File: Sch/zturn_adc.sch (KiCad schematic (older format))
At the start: 0 parts

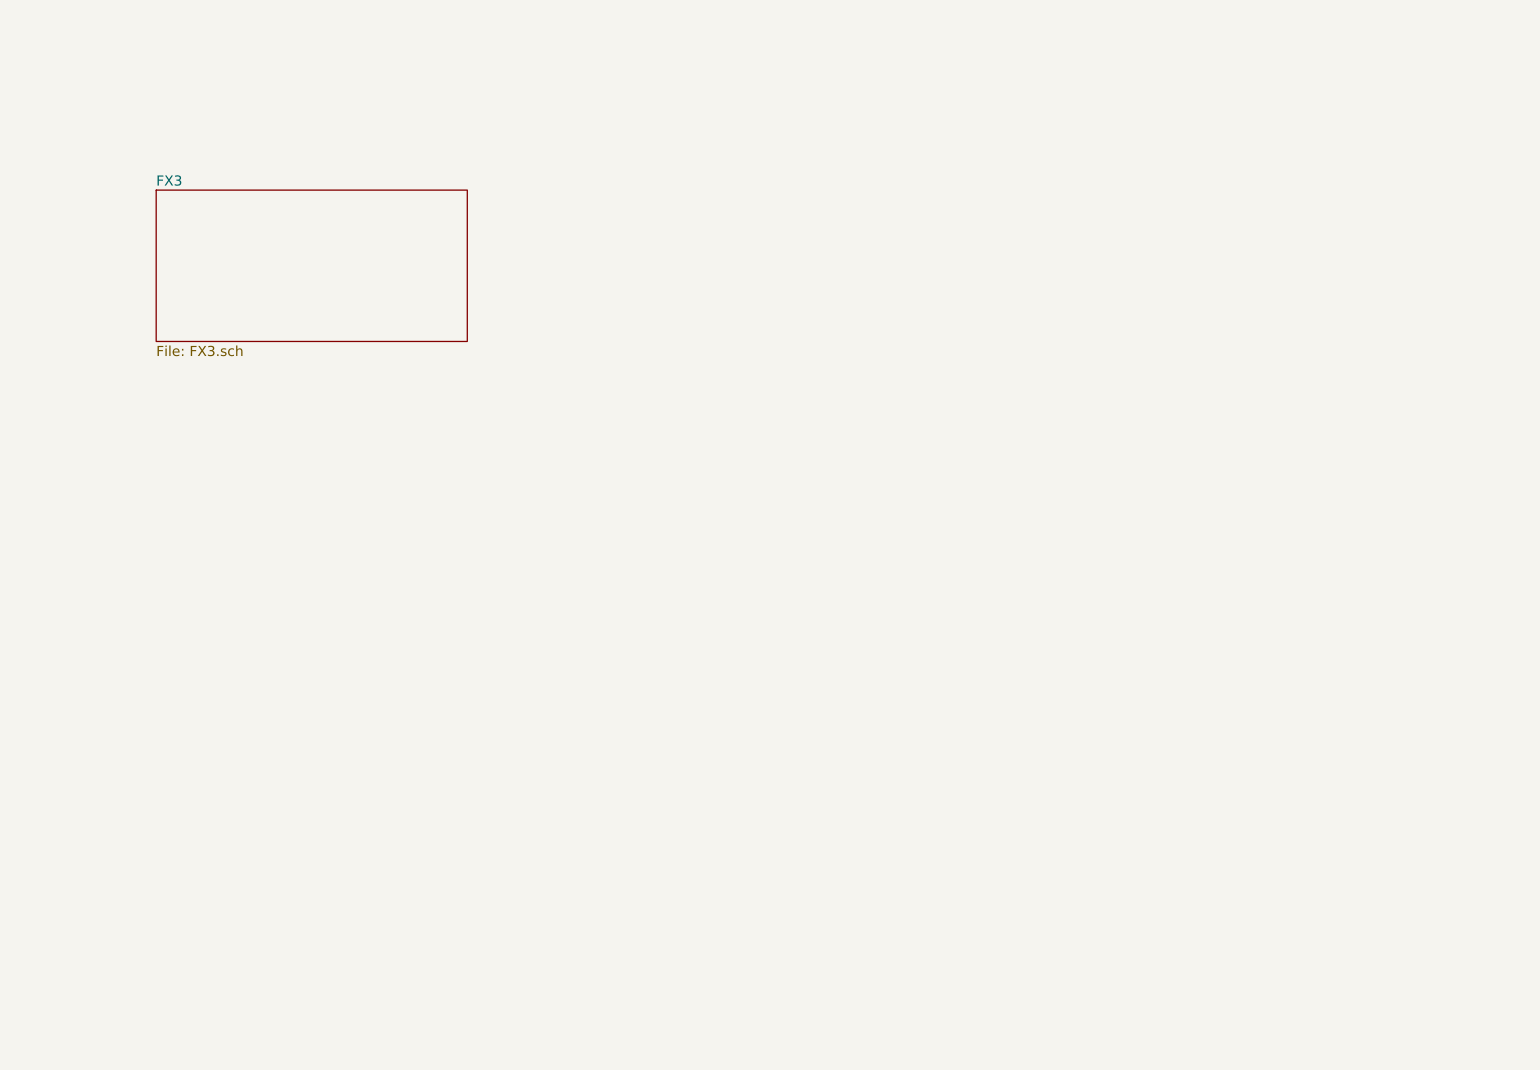
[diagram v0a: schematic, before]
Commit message: FX3 clock,reset,cn
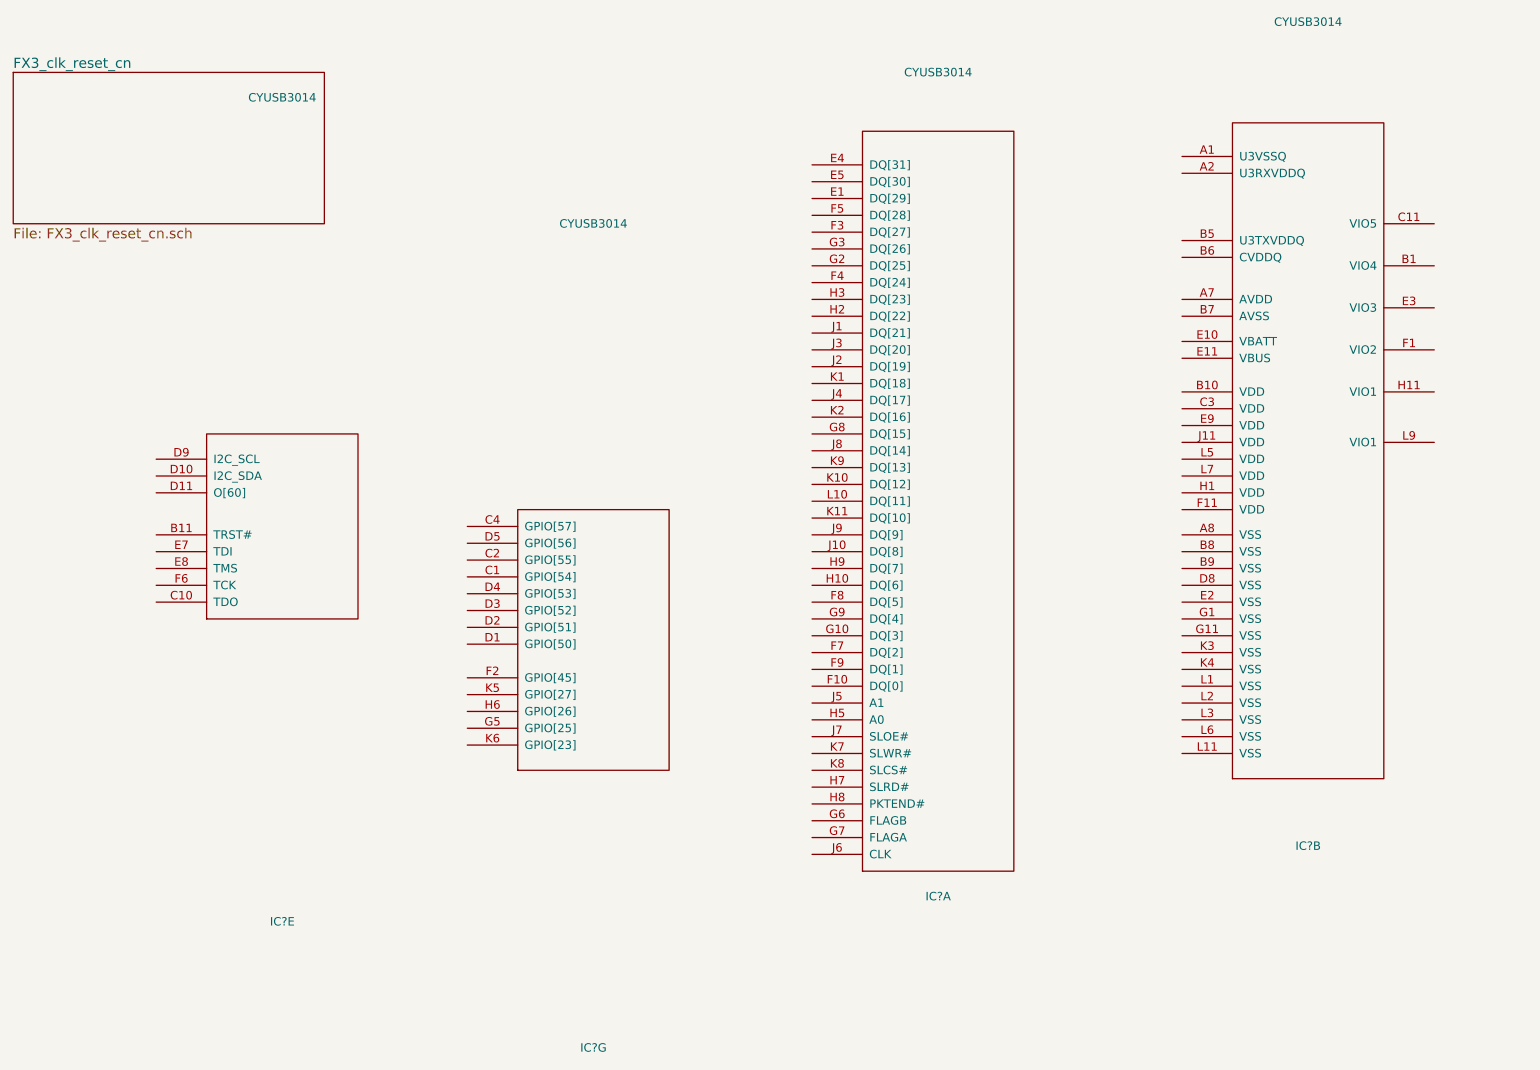
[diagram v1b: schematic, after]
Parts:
- added IC? (x4): CYUSB3014, MODULE, symbol CYUSB3014
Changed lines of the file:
@@
 LIBS:valves
 LIBS:zturn_adc
+LIBS:CYUSB3014
 LIBS:zturn_adc-cache
 EELAYER 25 0
@@
 $EndDescr
 $Sheet
-S 2100 1900 1850 900
+S 1250 1200 1850 900
 U 589ADF9D
-F0 "FX3" 60
-F1 "FX3.sch" 60
+F0 "FX3_clk_reset_cn" 60
+F1 "FX3_clk_reset_cn.sch" 60
 $EndSheet
+$Comp
+L CYUSB3014 IC?
+U 1 1 58A0A68D
+P 6750 3750
+F 0 "IC?" H 6750 1400 50  0000 C CNN
+F 1 "CYUSB3014" H 6750 6300 50  0000 C CNN
+F 2 "MODULE" H 6700 6050 50  0001 C CNN
+F 3 "DOCUMENTATION" H 6750 6200 50  0001 C CNN
+	1    6750 3750
+	1    0    0    -1
+$EndComp
+$Comp
+L CYUSB3014 IC?
+U 2 1 58A0A6C8
+P 8950 3450
+F 0 "IC?" H 8950 1100 50  0000 C CNN
+F 1 "CYUSB3014" H 8950 6000 50  0000 C CNN
+F 2 "MODULE" H 8900 5750 50  0001 C CNN
+F 3 "DOCUMENTATION" H 8950 5900 50  0001 C CNN
+	2    8950 3450
+	1    0    0    -1
+$EndComp
+$Comp
+L CYUSB3014 IC?
+U 5 1 58A0A752
+P 2850 3900
+F 0 "IC?" H 2850 1550 50  0000 C CNN
+F 1 "CYUSB3014" H 2850 6450 50  0000 C CNN
+F 2 "MODULE" H 2800 6200 50  0001 C CNN
+F 3 "DOCUMENTATION" H 2850 6350 50  0001 C CNN
+	5    2850 3900
+	1    0    0    -1
+$EndComp
+$Comp
+L CYUSB3014 IC?
+U 7 1 58A0A799
+P 4700 4650
+F 0 "IC?" H 4700 2300 50  0000 C CNN
+F 1 "CYUSB3014" H 4700 7200 50  0000 C CNN
+F 2 "MODULE" H 4650 6950 50  0001 C CNN
+F 3 "DOCUMENTATION" H 4700 7100 50  0001 C CNN
+	7    4700 4650
+	1    0    0    -1
+$EndComp
 $EndSCHEMATC

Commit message: Add DQ and 80-pin
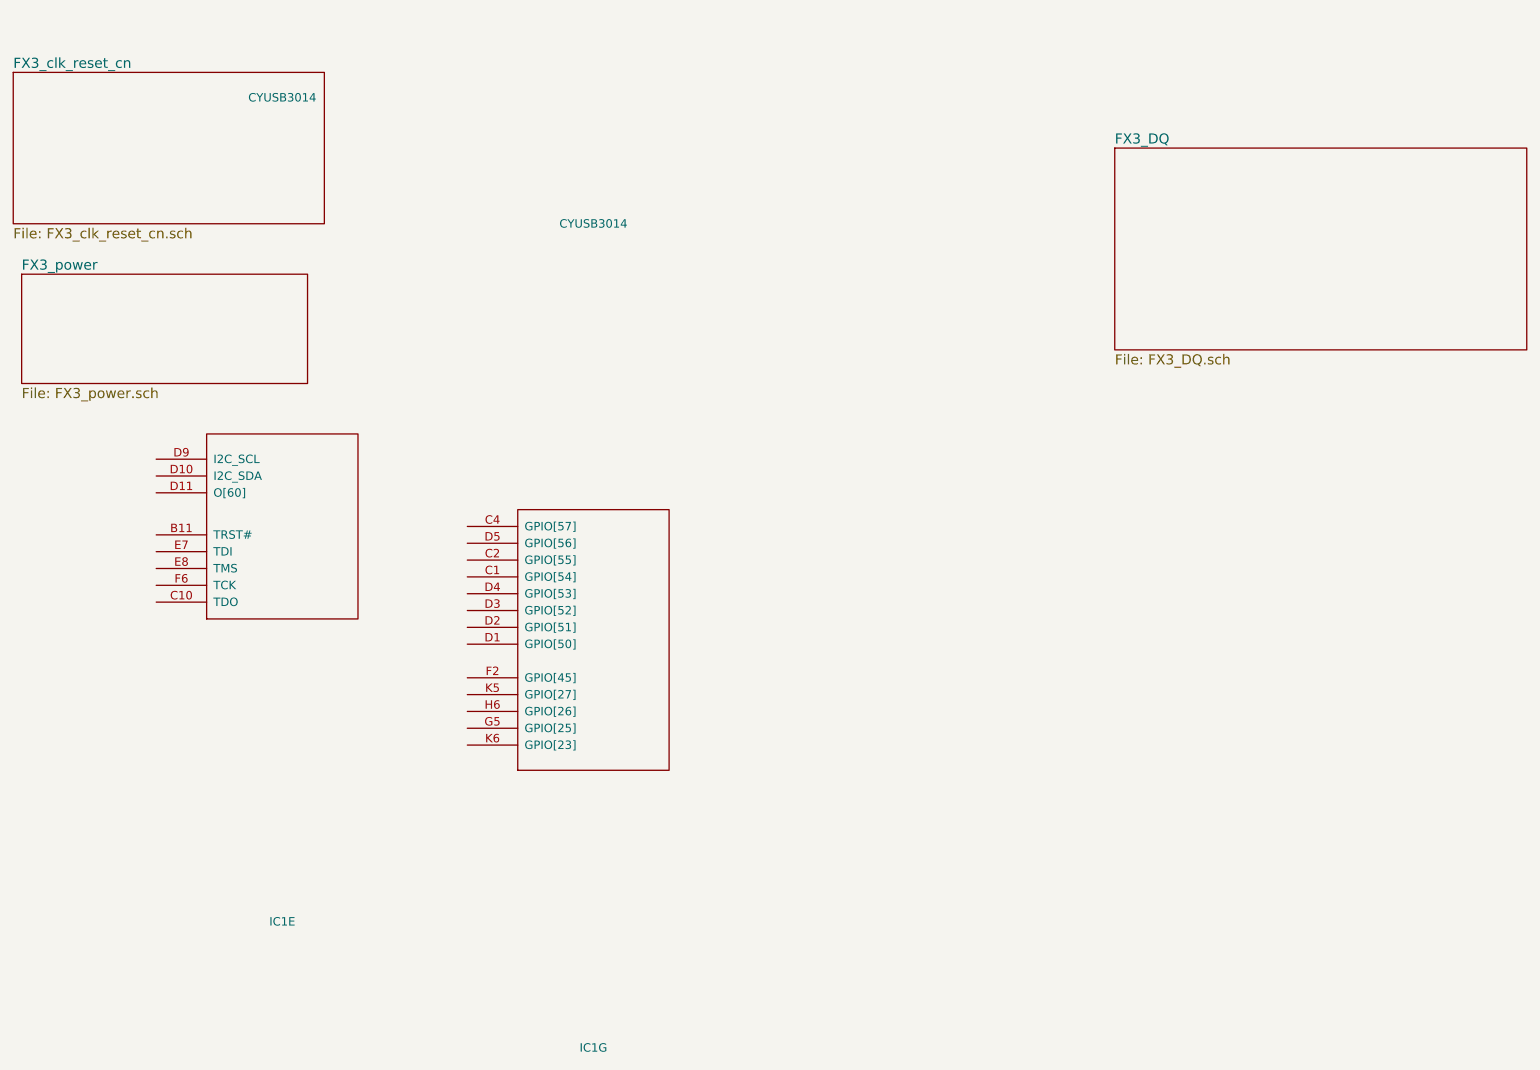
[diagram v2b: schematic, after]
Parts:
- removed IC? (x2): CYUSB3014, MODULE, symbol CYUSB3014
- gave numbers to parts that had none: 1
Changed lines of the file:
@@
 $Descr A4 11693 8268
 encoding utf-8
-Sheet 1 2
+Sheet 1 4
 Title ""
 Date ""
@@
 $EndSheet
 $Comp
-L CYUSB3014 IC?
-U 1 1 58A0A68D
-P 6750 3750
-F 0 "IC?" H 6750 1400 50  0000 C CNN
-F 1 "CYUSB3014" H 6750 6300 50  0000 C CNN
-F 2 "MODULE" H 6700 6050 50  0001 C CNN
-F 3 "DOCUMENTATION" H 6750 6200 50  0001 C CNN
-	1    6750 3750
-	1    0    0    -1
-$EndComp
-$Comp
-L CYUSB3014 IC?
-U 2 1 58A0A6C8
-P 8950 3450
-F 0 "IC?" H 8950 1100 50  0000 C CNN
-F 1 "CYUSB3014" H 8950 6000 50  0000 C CNN
-F 2 "MODULE" H 8900 5750 50  0001 C CNN
-F 3 "DOCUMENTATION" H 8950 5900 50  0001 C CNN
-	2    8950 3450
-	1    0    0    -1
-$EndComp
-$Comp
-L CYUSB3014 IC?
+L CYUSB3014 IC1
 U 5 1 58A0A752
 P 2850 3900
-F 0 "IC?" H 2850 1550 50  0000 C CNN
+F 0 "IC1" H 2850 1550 50  0000 C CNN
 F 1 "CYUSB3014" H 2850 6450 50  0000 C CNN
 F 2 "MODULE" H 2800 6200 50  0001 C CNN
@@
 $EndComp
 $Comp
-L CYUSB3014 IC?
+L CYUSB3014 IC1
 U 7 1 58A0A799
 P 4700 4650
-F 0 "IC?" H 4700 2300 50  0000 C CNN
+F 0 "IC1" H 4700 2300 50  0000 C CNN
 F 1 "CYUSB3014" H 4700 7200 50  0000 C CNN
 F 2 "MODULE" H 4650 6950 50  0001 C CNN
@@
 	1    0    0    -1
 $EndComp
+$Sheet
+S 1300 2400 1700 650
+U 58A06B55
+F0 "FX3_power" 60
+F1 "FX3_power.sch" 60
+$EndSheet
+$Sheet
+S 7800 1650 2450 1200
+U 58A0A991
+F0 "FX3_DQ" 60
+F1 "FX3_DQ.sch" 60
+$EndSheet
 $EndSCHEMATC
